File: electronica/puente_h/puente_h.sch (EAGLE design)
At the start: 46 parts, among them IC1 7805, IC2 7812, IC3 74HC04N, IC4 74HC08N, Q1 IRF2804, Q2 IRF2804, Q5 IRF2804, Q6 IRF2804, U1 IR211014LEAD, U3 IR211014LEAD

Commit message: test viernes, esquematico con nuevo optoacoplador
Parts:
- removed JP1: (no value), pinhead:PINHD-1X5
- removed R10, R11, R12, R9: 470, rcl:R-EU_0207/12
- removed R6, R7, R8: 220, rcl:R-EU_0207/12
- removed U1: IR211014LEAD, components:IR211014LEAD
- added C11: 0.1u, rcl:C-EUC3216
- added IC5: ADUM1400, adum140x:ADUM1400
- added JP2: (no value), pinhead:PINHD-1X6
- C7: value (none) -> 0.1u; device rcl:CPOL-EUE7.5-16 -> rcl:C-EUC3216
- C8: value (none) -> 2200u
- R5: value 220 -> 1k
- U$1: value PS2501-4 -> IR2110; device components:PS2501-4 -> components:IR2110
- U3: value IR211014LEAD -> IR2110; device components:IR211014LEAD -> components:IR2110
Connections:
- removed net N$19 (its old number): JP1.3, R7.1
- removed net N$20: JP1.4, R8.1
- removed net N$21: JP1.5, U$1.P$2, U$1.P$4, U$1.P$6, U$1.P$8
- removed net N$22: IC3C.O
- new net GND1@2: C7.2, IC5.GND1@1, IC5.GND1@2, JP2.2
- new net N$5: C7.1, IC5.VDD1, JP2.1
- new net N$8: IC5.VIA, JP2.3
- net +12V: now also C1.1, IC1.IN, U$1.VCC; no longer U$1.P$10, U$1.P$12, U$1.P$14, U$1.P$16, U1.VCC
- net +5V: now also C11.2, IC3P.VCC, IC4P.VCC, IC5.VDD2, R5.2, U$1.VDD; no longer U1.VDD
- net A: now also IC5.VOB; no longer R9.2, U$1.P$13
- net B: now also IC5.VOC; no longer R11.2, U$1.P$11
- net EN: now also IC5.VOA; no longer R10.2, U$1.P$15
- net GND: now also C11.1, IC3P.GND, IC4P.GND, IC5.GND2@1, IC5.GND2@2, U$1.COM, U$1.VSS; no longer C7.-, R10.1, R11.1, R12.1, R9.1, U1.COM, U1.VSS
- net N$1: now also U$1.VB; no longer U1.VB
- net N$11: now also U$1.HIN; no longer U1.HIN
- net N$12: now also U$1.LIN
- net N$13: now also IC5.VIB, JP2.4; no longer R5.2, U$1.P$1
- net N$14: now also IC5.VIC, JP2.5; no longer R6.2, U$1.P$3
- net N$15: now also IC5.VID, JP2.6; no longer R7.2, U$1.P$5
- net N$16: now also IC5.VE2, R5.1; no longer R8.2, U$1.P$7
- net N$17: now also IC3C.O, IC4D.I1; no longer JP1.1, R5.1
- net N$18: now also IC3B.I, IC5.VOD; no longer JP1.2, R6.1
- net N$2: now also U$1.HO; no longer U1.HO
- net N$3: now also U$1.VS; no longer U1.VS
- net N$6: now also U$1.LO; no longer U1.LO
- net SD: now also IC3B.O, U$1.SD; no longer R12.2, U$1.P$9, U1.SD
- net VIN: now also Q1.D, Q5.D; no longer C1.1, C7.+, IC1.IN
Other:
- moved on the sheet: R5

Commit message: pads mas largos
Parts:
- removed JP2: (no value), pinhead:PINHD-1X6
- removed U3: IR2110, components:IR2110
- added JP1: (no value), pinhead:PINHD-1X6
- added U1: IR2110LP, components:IR2110LP
- U$1: value IR2110 -> IR2110LP; device components:IR2110 -> components:IR2110LP
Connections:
- removed net GND1@2: C7.2, IC5.GND1@1, IC5.GND1@2, JP2.2
- removed net N$13: IC5.VIB, JP2.4
- removed net N$14: IC5.VIC, JP2.5
- removed net N$8: IC5.VIA, JP2.3
- new net N$20: IC5.VID, JP1.1
- new net N$21: IC5.VIB, JP1.3
- new net N$22: IC5.VIA, JP1.4
- new net N$24: C7.1, IC5.VDD1, JP1.6
- net +12V: now also U1.VCC; no longer U3.VCC
- net +5V: now also U1.VDD; no longer U3.VDD
- net GND: now also U1.COM, U1.VSS; no longer U3.COM, U3.VSS
- net N$1: now also U1.VB; no longer U$1.VB
- net N$11: now also U1.HIN; no longer U$1.HIN
- net N$12: now also U1.LIN; no longer U$1.LIN
- net N$15: now also IC5.VIC, JP1.2; no longer IC5.VID, JP2.6
- net N$19: now also U$1.LIN; no longer U3.LIN
- net N$2: now also U1.HO; no longer U$1.HO
- net N$3: now also U1.VS; no longer U$1.VS
- net N$30: now also U$1.VB; no longer U3.VB
- net N$31: now also U$1.VS; no longer U3.VS
- net N$32: now also U$1.HO; no longer U3.HO
- net N$35: now also U$1.LO; no longer U3.LO
- net N$5: now also C7.2, IC5.GND1@1, IC5.GND1@2, JP1.5; no longer C7.1, IC5.VDD1, JP2.1
- net N$6: now also U1.LO; no longer U$1.LO
- net N$9: now also U$1.HIN; no longer U3.HIN
- net SD: now also U1.SD; no longer U3.SD
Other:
- moved on the sheet: U$1

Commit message: packages con pad mas largos, nuevo pcb
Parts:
- IC3: value 74HC04N -> 7404LP; device 74xx-eu:74HC04N -> components:7404LP
- IC4: value 74HC08N -> 7408LP; device 74xx-eu:74HC08N -> components:7408LP
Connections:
- net A: now also IC3C.I; no longer IC3A.I
- net B: now also IC3F.I; no longer IC3C.I
- net N$10: now also IC3C.O; no longer IC3A.O
- net N$17: now also IC3F.O; no longer IC3C.O
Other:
- moved on the sheet: IC3C
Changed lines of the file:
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@@
 <part name="R2" library="rcl" deviceset="R-EU_" device="0207/12" value="1k"/>
 <part name="GND3" library="supply1" deviceset="GND" device=""/>
-<part name="IC3" library="74xx-eu" deviceset="74*04" device="N" technology="HC"/>
-<part name="IC4" library="74xx-eu" deviceset="74*08" device="N" technology="HC"/>
+<part name="IC3" library="components" deviceset="74*04" device="LP"/>
+<part name="IC4" library="components" deviceset="74*08" device="LP"/>
 <part name="P+4" library="supply1" deviceset="+5V" device=""/>
 <part name="P+8" library="supply1" deviceset="+12V" device=""/>
@@
 <instance part="R2" gate="G$1" x="153.67" y="-36.83"/>
 <instance part="GND3" gate="1" x="78.74" y="-27.94"/>
-<instance part="IC3" gate="A" x="7.62" y="5.08"/>
-<instance part="IC3" gate="C" x="354.33" y="5.08" rot="R180"/>
+<instance part="IC3" gate="C" x="7.62" y="5.08"/>
+<instance part="IC3" gate="F" x="354.33" y="5.08" rot="R180"/>
 <instance part="IC4" gate="A" x="53.34" y="10.16"/>
 <instance part="IC4" gate="B" x="33.02" y="2.54"/>
@@
 <net name="N$10" class="0">
 <segment>
-<pinref part="IC3" gate="A" pin="O"/>
+<pinref part="IC3" gate="C" pin="O"/>
 <pinref part="IC4" gate="B" pin="I0"/>
 <wire x1="17.78" y1="5.08" x2="25.4" y2="5.08" width="0.1524" layer="91"/>
@@
 <net name="A" class="0">
 <segment>
-<pinref part="IC3" gate="A" pin="I"/>
+<pinref part="IC3" gate="C" pin="I"/>
 <wire x1="-2.54" y1="5.08" x2="-5.08" y2="5.08" width="0.1524" layer="91"/>
 <wire x1="-5.08" y1="5.08" x2="-5.08" y2="12.7" width="0.1524" layer="91"/>
@@
 <net name="B" class="0">
 <segment>
-<pinref part="IC3" gate="C" pin="I"/>
+<pinref part="IC3" gate="F" pin="I"/>
 <wire x1="364.49" y1="5.08" x2="370.84" y2="5.08" width="0.1524" layer="91"/>
 <wire x1="370.84" y1="5.08" x2="370.84" y2="12.7" width="0.1524" layer="91"/>
@@
 <segment>
 <pinref part="IC4" gate="D" pin="I1"/>
-<pinref part="IC3" gate="C" pin="O"/>
+<pinref part="IC3" gate="F" pin="O"/>
 <wire x1="339.09" y1="5.08" x2="344.17" y2="5.08" width="0.1524" layer="91"/>
 </segment>

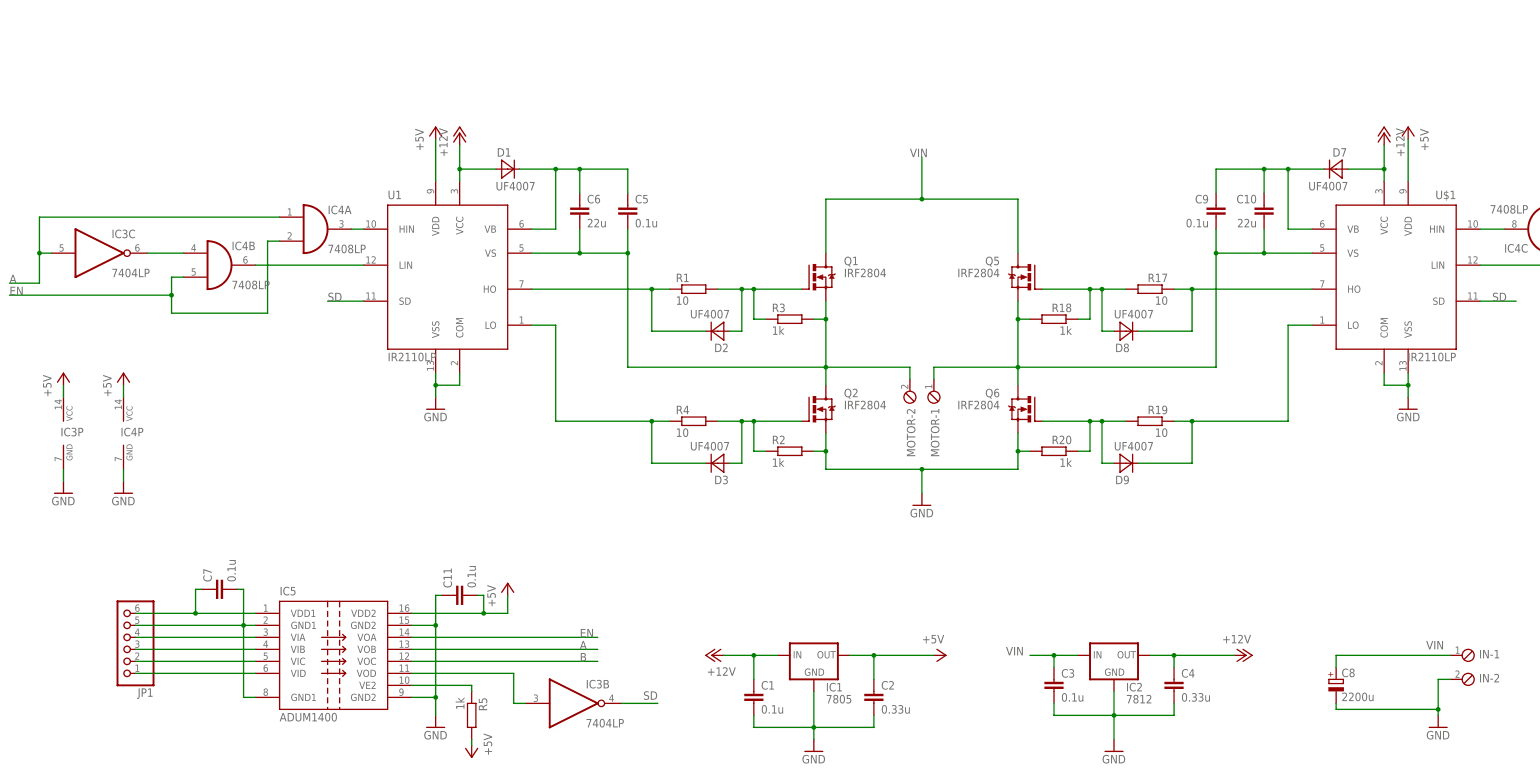
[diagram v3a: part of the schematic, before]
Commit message: ruteo con poligonos
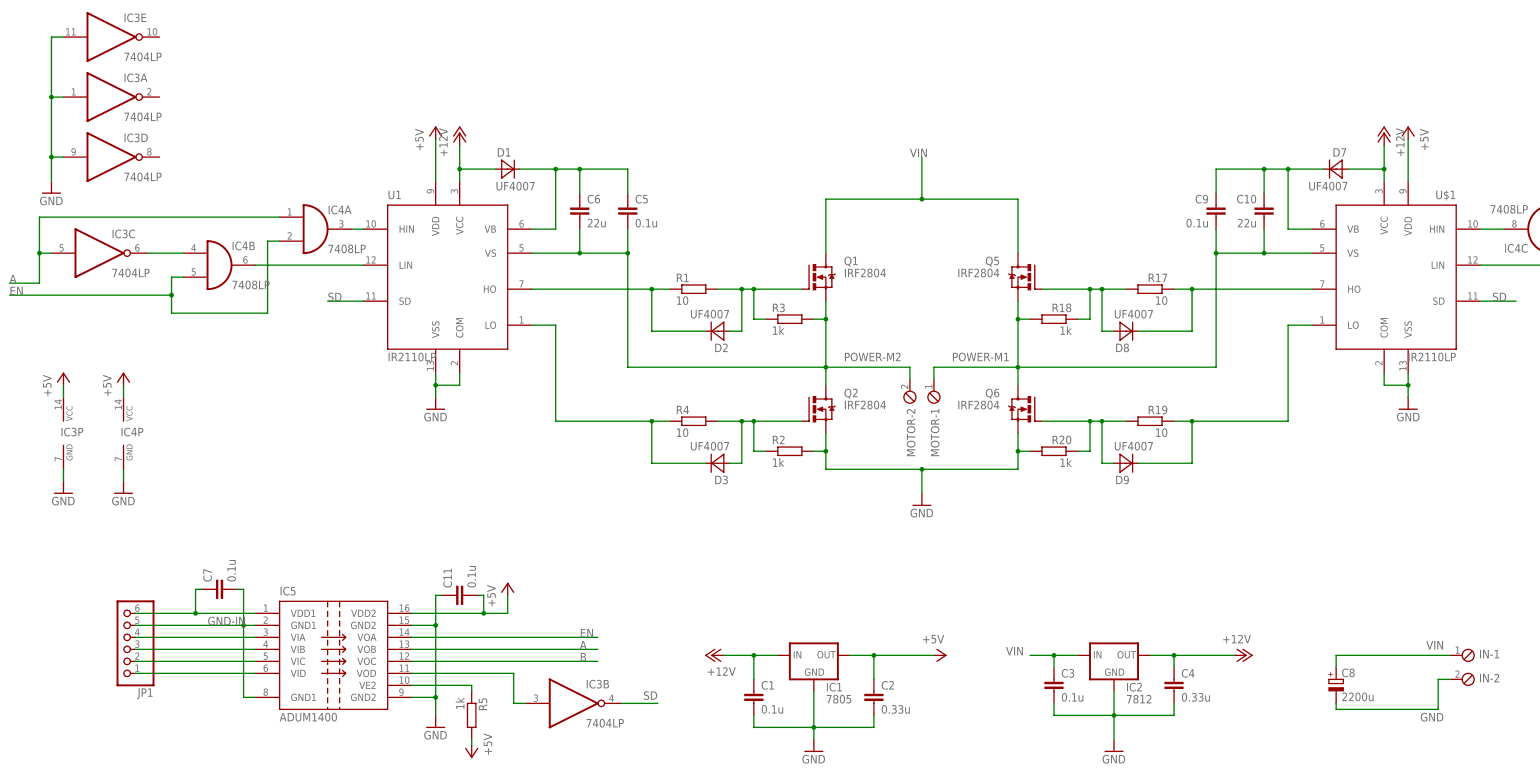
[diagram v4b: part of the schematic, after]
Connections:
- net N$3 renamed POWER-M2
- net N$31 renamed POWER-M1
- net N$5 renamed GND-IN
- net GND: now also IC3A.I, IC3D.I, IC3E.I
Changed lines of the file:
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@@
 <part name="GND5" library="supply1" deviceset="GND" device=""/>
 <part name="IN" library="con-phoenix-254" deviceset="MPT2" device=""/>
-<part name="GND7" library="supply1" deviceset="GND" device=""/>
 <part name="C8" library="rcl" deviceset="CPOL-EU" device="E7.5-16" value="2200u"/>
 <part name="MOTOR" library="con-phoenix-254" deviceset="MPT2" device=""/>
@@
 <part name="U1" library="components" deviceset="IR2110" device="LP"/>
 <part name="U$1" library="components" deviceset="IR2110" device="LP"/>
+<part name="GND7" library="supply1" deviceset="GND" device=""/>
 </parts>
 <sheets>
@@
 <instance part="IN" gate="-1" x="295.91" y="-80.01"/>
 <instance part="IN" gate="-2" x="295.91" y="-85.09"/>
-<instance part="GND7" gate="1" x="290.83" y="-95.25"/>
 <instance part="C8" gate="G$1" x="269.24" y="-85.09"/>
 <instance part="MOTOR" gate="-1" x="184.15" y="-24.13" rot="R270"/>
@@
 <instance part="U1" gate="G$1" x="83.82" y="0"/>
 <instance part="U$1" gate="G$1" x="279.4" y="0" rot="MR0"/>
+<instance part="IC3" gate="A" x="10.16" y="38.1"/>
+<instance part="IC3" gate="D" x="10.16" y="25.4"/>
+<instance part="IC3" gate="E" x="10.16" y="50.8"/>
+<instance part="GND7" gate="1" x="-2.54" y="17.78"/>
 </instances>
 <busses>
@@
 </segment>
 <segment>
-<pinref part="IN" gate="-2" pin="1"/>
-<pinref part="GND7" gate="1" pin="GND"/>
-<wire x1="293.37" y1="-85.09" x2="290.83" y2="-85.09" width="0.1524" layer="91"/>
-<wire x1="290.83" y1="-85.09" x2="290.83" y2="-91.44" width="0.1524" layer="91"/>
-<pinref part="C8" gate="G$1" pin="-"/>
-<wire x1="290.83" y1="-91.44" x2="290.83" y2="-92.71" width="0.1524" layer="91"/>
-<wire x1="269.24" y1="-90.17" x2="269.24" y2="-91.44" width="0.1524" layer="91"/>
-<wire x1="269.24" y1="-91.44" x2="290.83" y2="-91.44" width="0.1524" layer="91"/>
-<junction x="290.83" y="-91.44"/>
-</segment>
-<segment>
 <pinref part="GND9" gate="1" pin="GND"/>
 <pinref part="IC4" gate="P" pin="GND"/>
@@
 <wire x1="78.74" y1="-67.31" x2="78.74" y2="-73.66" width="0.1524" layer="91"/>
 <junction x="78.74" y="-73.66"/>
+</segment>
+<segment>
+<pinref part="IN" gate="-2" pin="1"/>
+<wire x1="293.37" y1="-85.09" x2="290.83" y2="-85.09" width="0.1524" layer="91"/>
+<wire x1="290.83" y1="-85.09" x2="290.83" y2="-91.44" width="0.1524" layer="91"/>
+<pinref part="C8" gate="G$1" pin="-"/>
+<wire x1="269.24" y1="-90.17" x2="269.24" y2="-91.44" width="0.1524" layer="91"/>
+<wire x1="269.24" y1="-91.44" x2="290.83" y2="-91.44" width="0.1524" layer="91"/>
+<label x="287.02" y="-93.98" size="1.778" layer="95"/>
+</segment>
+<segment>
+<pinref part="IC3" gate="E" pin="I"/>
+<wire x1="0" y1="50.8" x2="-2.54" y2="50.8" width="0.1524" layer="91"/>
+<wire x1="-2.54" y1="50.8" x2="-2.54" y2="38.1" width="0.1524" layer="91"/>
+<pinref part="IC3" gate="D" pin="I"/>
+<wire x1="-2.54" y1="38.1" x2="-2.54" y2="25.4" width="0.1524" layer="91"/>
+<wire x1="-2.54" y1="25.4" x2="0" y2="25.4" width="0.1524" layer="91"/>
+<pinref part="IC3" gate="A" pin="I"/>
+<wire x1="0" y1="38.1" x2="-2.54" y2="38.1" width="0.1524" layer="91"/>
+<junction x="-2.54" y="38.1"/>
+<wire x1="-2.54" y1="25.4" x2="-2.54" y2="20.32" width="0.1524" layer="91"/>
+<pinref part="GND7" gate="1" pin="GND"/>
+<junction x="-2.54" y="25.4"/>
 </segment>
 </net>
@@
 </segment>
 </net>
-<net name="N$3" class="0">
+<net name="POWER-M2" class="0">
 <segment>
 <wire x1="119.38" y1="-19.05" x2="161.29" y2="-19.05" width="0.1524" layer="91"/>
@@
 <wire x1="161.29" y1="-19.05" x2="161.29" y2="-8.89" width="0.1524" layer="91"/>
 <pinref part="U1" gate="G$1" pin="VS"/>
+<label x="165.1" y="-17.78" size="1.778" layer="95"/>
 </segment>
 </net>
@@
 </segment>
 </net>
-<net name="N$31" class="0">
+<net name="POWER-M1" class="0">
 <segment>
 <wire x1="243.84" y1="-19.05" x2="201.93" y2="-19.05" width="0.1524" layer="91"/>
@@
 <wire x1="201.93" y1="-19.05" x2="201.93" y2="-8.89" width="0.1524" layer="91"/>
 <pinref part="U$1" gate="G$1" pin="VS"/>
+<label x="187.96" y="-17.78" size="1.778" layer="95"/>
 </segment>
 </net>
@@
 </segment>
 </net>
-<net name="N$5" class="0">
+<net name="GND-IN" class="0">
 <segment>
 <pinref part="IC5" gate="G$1" pin="GND1@1"/>
@@
 <pinref part="C7" gate="G$1" pin="2"/>
 <pinref part="JP1" gate="A" pin="5"/>
-</segment>
-</net>
+<label x="30.48" y="-73.66" size="1.778" layer="95"/>
+</segment>
+</net>

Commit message: placas nuevas
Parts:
- removed IN, MOTOR: (no value), con-phoenix-254:MPT2
- added CON-IN, CON-MOTOR: METALTEX-2, components:METALTEX-2
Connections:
- net GND: now also CON-IN.P2; no longer IN-2.1
- net POWER-M1: now also CON-MOTOR.P2; no longer MOTOR-1.1
- net POWER-M2: now also CON-MOTOR.P1; no longer MOTOR-2.1
- net VIN: now also CON-IN.P1; no longer IN-1.1
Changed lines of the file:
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@@
 <setting verticaltext="up"/>
 </settings>
-<grid distance="0.1" unitdist="inch" unit="inch" style="lines" multiple="1" display="no" altdistance="0.01" altunitdist="inch" altunit="inch"/>
+<grid distance="0.01" unitdist="inch" unit="inch" style="lines" multiple="1" display="no" altdistance="0.01" altunitdist="inch" altunit="inch"/>
 <layers>
 <layer number="1" name="Top" color="4" fill="1" visible="no" active="no"/>
+<layer number="2" name="Route2" color="1" fill="3" visible="no" active="no"/>
+<layer number="3" name="Route3" color="4" fill="3" visible="no" active="no"/>
+<layer number="4" name="Route4" color="1" fill="4" visible="no" active="no"/>
+<layer number="5" name="Route5" color="4" fill="4" visible="no" active="no"/>
+<layer number="6" name="Route6" color="1" fill="8" visible="no" active="no"/>
+<layer number="7" name="Route7" color="4" fill="8" visible="no" active="no"/>
+<layer number="8" name="Route8" color="1" fill="2" visible="no" active="no"/>
+<layer number="9" name="Route9" color="4" fill="2" visible="no" active="no"/>
+<layer number="10" name="Route10" color="1" fill="7" visible="no" active="no"/>
+<layer number="11" name="Route11" color="4" fill="7" visible="no" active="no"/>
+<layer number="12" name="Route12" color="1" fill="5" visible="no" active="no"/>
+<layer number="13" name="Route13" color="4" fill="5" visible="no" active="no"/>
+<layer number="14" name="Route14" color="1" fill="6" visible="no" active="no"/>
+<layer number="15" name="Route15" color="4" fill="6" visible="no" active="no"/>
 <layer number="16" name="Bottom" color="1" fill="1" visible="no" active="no"/>
 <layer number="17" name="Pads" color="2" fill="1" visible="no" active="no"/>
@@
 <part name="P+9" library="supply1" deviceset="+5V" device=""/>
 <part name="GND5" library="supply1" deviceset="GND" device=""/>
-<part name="IN" library="con-phoenix-254" deviceset="MPT2" device=""/>
 <part name="C8" library="rcl" deviceset="CPOL-EU" device="E7.5-16" value="2200u"/>
-<part name="MOTOR" library="con-phoenix-254" deviceset="MPT2" device=""/>
 <part name="IC5" library="adum140x" deviceset="ADUM1400" device=""/>
 <part name="GND4" library="supply1" deviceset="GND" device=""/>
@@
 <part name="U$1" library="components" deviceset="IR2110" device="LP"/>
 <part name="GND7" library="supply1" deviceset="GND" device=""/>
+<part name="CON-IN" library="components" deviceset="METALTEX-2" device=""/>
+<part name="CON-MOTOR" library="components" deviceset="METALTEX-2" device=""/>
 </parts>
 <sheets>
@@
 <instance part="P+9" gate="1" x="284.48" y="31.75" rot="MR0"/>
 <instance part="GND5" gate="1" x="181.61" y="-48.26"/>
-<instance part="IN" gate="-1" x="295.91" y="-80.01"/>
-<instance part="IN" gate="-2" x="295.91" y="-85.09"/>
 <instance part="C8" gate="G$1" x="269.24" y="-85.09"/>
-<instance part="MOTOR" gate="-1" x="184.15" y="-24.13" rot="R270"/>
-<instance part="MOTOR" gate="-2" x="179.07" y="-24.13" rot="R270"/>
 <instance part="IC5" gate="G$1" x="55.88" y="-78.74"/>
 <instance part="GND4" gate="1" x="78.74" y="-95.25"/>
@@
 <instance part="IC3" gate="E" x="10.16" y="50.8"/>
 <instance part="GND7" gate="1" x="-2.54" y="17.78"/>
+<instance part="CON-IN" gate="G$1" x="300.99" y="-80.01"/>
+<instance part="CON-MOTOR" gate="G$1" x="179.07" y="-10.16" rot="R90"/>
 </instances>
 <busses>
@@
 </segment>
 <segment>
-<pinref part="IN" gate="-2" pin="1"/>
 <wire x1="293.37" y1="-85.09" x2="290.83" y2="-85.09" width="0.1524" layer="91"/>
 <wire x1="290.83" y1="-85.09" x2="290.83" y2="-91.44" width="0.1524" layer="91"/>
@@
 <wire x1="269.24" y1="-91.44" x2="290.83" y2="-91.44" width="0.1524" layer="91"/>
 <label x="287.02" y="-93.98" size="1.778" layer="95"/>
+<pinref part="CON-IN" gate="G$1" pin="P2"/>
 </segment>
 <segment>
@@
 </segment>
 <segment>
-<pinref part="IN" gate="-1" pin="1"/>
 <wire x1="293.37" y1="-80.01" x2="269.24" y2="-80.01" width="0.1524" layer="91"/>
 <pinref part="C8" gate="G$1" pin="+"/>
 <wire x1="269.24" y1="-80.01" x2="269.24" y2="-82.55" width="0.1524" layer="91"/>
 <label x="288.29" y="-78.74" size="1.778" layer="95"/>
+<pinref part="CON-IN" gate="G$1" pin="P1"/>
 </segment>
 </net>
@@
 <junction x="119.38" y="5.08"/>
 <junction x="109.22" y="5.08"/>
-<pinref part="MOTOR" gate="-2" pin="1"/>
-<wire x1="179.07" y1="-21.59" x2="179.07" y2="-19.05" width="0.1524" layer="91"/>
 <pinref part="R3" gate="G$1" pin="2"/>
 <pinref part="Q1" gate="G$1" pin="S"/>
@@
 <pinref part="U1" gate="G$1" pin="VS"/>
 <label x="165.1" y="-17.78" size="1.778" layer="95"/>
+<pinref part="CON-MOTOR" gate="G$1" pin="P1"/>
+<wire x1="179.07" y1="-19.05" x2="179.07" y2="-17.78" width="0.1524" layer="91"/>
 </segment>
 </net>
@@
 <junction x="243.84" y="5.08"/>
 <junction x="254" y="5.08"/>
-<pinref part="MOTOR" gate="-1" pin="1"/>
-<wire x1="184.15" y1="-21.59" x2="184.15" y2="-19.05" width="0.1524" layer="91"/>
 <pinref part="R18" gate="G$1" pin="2"/>
 <pinref part="Q5" gate="G$1" pin="S"/>
@@
 <pinref part="U$1" gate="G$1" pin="VS"/>
 <label x="187.96" y="-17.78" size="1.778" layer="95"/>
-</segment>
-</net>
+<pinref part="CON-MOTOR" gate="G$1" pin="P2"/>
+<wire x1="184.15" y1="-19.05" x2="184.15" y2="-17.78" width="0.1524" layer="91"/>
+</segment>
+</net>
